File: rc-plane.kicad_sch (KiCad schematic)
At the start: 146 parts, among them IC1 ISLA85005A, IC2 ISLA85005A, J1 POWER, J2 ARMING_PLUG, J3 SMA, J4 E-MATCH_DROGUE, J5 SWD, J6 E-MATCH_RECOVERY, J8 E-MATCH_DROGUE, J9 E-MATCH_RECOVERY, M1 MG90S, M2 MG90S, M3 MG90S, M4 MG90S, M5 MG90S, M6 MG90S, Q1 Q_NMOS_GSD, Q2 Q_NMOS_GSD, Q3 BC547, Q4 Q_NMOS_GSD, Q5 Q_NMOS_GSD, Q6 Q_NMOS_GSD, Q7 Q_NMOS_GSD, Q8 Q_NMOS_GSD, Q9 Q_NMOS_GSD, U1 STM32G474VET6, U5 MP1584EN-LF-Z, U8 MMC5983MA, U9 USBLC6-2SC6, Y1 16MHz

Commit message: Mostly done with schematic, need to do review
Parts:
- removed C2, C3: 100nF, Capacitor_SMD:C_0603_1608Metric, symbol Device:C_Small
- removed C27: 10uF, Capacitor_SMD:C_0603_1608Metric, symbol Device:C
- removed C30, C33: 100nF, Capacitor_SMD:C_0603_1608Metric, symbol Device:C
- removed J9: E-MATCH_RECOVERY, TerminalBlock:TerminalBlock_bornier-2_P5.08mm, symbol Connector:Conn_01x02_Socket
- removed M1, M2, M3, M4, M5, M6: MG90S, Connector_PinHeader_2.54mm:PinHeader_1x03_P2.54mm_Vertical, symbol Motor:Motor_Servo
- removed Q8, Q9: Q_NMOS_GSD, Package_TO_SOT_SMD:TSOT-23, symbol Device:Q_NMOS_GSD
- removed U1: STM32G474VET6, STM32G474VET6:QFP50P1600X1600X160-100N, symbol STM32G474VET6:STM32G474VET6
- removed U8: MMC5983MA, MMC5983MA:PQFN50P300X300X100-16N, symbol MMC5983MA:MMC5983MA
- added C117: 2.2uF, Capacitor_SMD:C_0402_1005Metric, symbol Device:C_Small
- added C27, C30: 100nF, Capacitor_SMD:C_0402_1005Metric, symbol Device:C_Small
- added C33, C42: 100nF, Capacitor_SMD:C_0603_1608Metric, symbol Device:C_Small
- added D10: BLUE, Diode_SMD:D_0603_1608Metric, symbol Device:LED
- added D15, D16: RED_LED, Diode_SMD:D_0603_1608Metric, symbol Device:LED
- added J9: HTSW-109-08-T-T-RA, UCIRP-KiCAD-Lib:SAMTEC_HTSW-109-08-T-T-RA, symbol UCIRP-KiCAD-Lib:HTSW-109-08-T-T-RA
- added U10: RASPBERRY_PI_4B_4GB, UCIRP-KiCAD-Lib:MODULE_RASPBERRY_PI_4B_4GB, symbol UCIRP-KiCAD-Lib:RASPBERRY_PI_4B_4GB
- added U11: ~, Package_QFP:LQFP-64_10x10mm_P0.5mm, symbol UCIRP-KiCAD-Lib:STM32F105RCT6
- added U8: BMM350, 0UCIRP-KiCAD-Lib:BMM350, symbol 0UCIRP-KiCAD-Lib:BMM350
- C34: value 120000uF -> 100nF
- J1: footprint Connector_AMASS:AMASS_XT60-M_1x02_P7.20mm_Vertical -> Connector_AMASS:AMASS_XT60PW-M_1x02_P7.20mm_Horizontal
- R12: value 100k -> 470; Manufacturer (none) -> Generic; Part # (none) -> Generic 0603 470 1% Resistor
- R27, R30: footprint Resistor_SMD:R_0603_1608Metric -> Resistor_SMD:R_0402_1005Metric; Manufacturer (none) -> Generic; Part # (none) -> Generic RES SMD 4.7K OHM 1% 1/4W 0402
- R3: value 3k -> 6k
- R32: value 10k -> 470; footprint (none) -> Resistor_SMD:R_0603_1608Metric; Manufacturer (none) -> Generic; Part # (none) -> Generic 0603 470 1% Resistor
- R40: value 10k -> 100k; Part # Generic 0603 10k 1% Resistor -> Generic 0603 1k 1% Resistor
- R41: value 100 -> 100k; Part # Generic 0603 100 1% Resistor -> Generic 0603 1k 1% Resistor
- R42: value 1 -> 100k; footprint (none) -> Resistor_SMD:R_0603_1608Metric; Manufacturer (none) -> Generic; Part # (none) -> Generic 0603 1k 1% Resistor
- R43: value 10k -> 100k; Manufacturer Generic -> (none); Part # Generic 0603 10k 1% Resistor -> (none)
- R44: value 1k -> 470; Part # Generic 0603 1k 1% Resistor -> Generic 0603 470 1% Resistor
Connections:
- net RADIO_MISO is gone; now on net MEM_MISO: U2.2 (MISO)
- net RADIO_MOSI is gone; now on net MEM_MOSI: U2.3 (MOSI)
- net RADIO_SCK is gone; now on net MEM_SCK: U2.4 (SCK)
- net +3.3V: now also C34.1, R40.2, R41.2, R42.2, R43.2, C27.1, C30.1, C33.1, J9.23, J9.26, U11.1 (VBAT), U11.13 (VDDA), U11.19 (VDD), U11.32 (VDD), U11.48 (VDD), U11.64 (VDD), U8.B3 (VDDIO), U8.C1 (VDD); no longer R12.2, R44.1
- net +5V: now also U10.2 (5V), U10.4 (5V); no longer C10.2, C19.1, C21.1, L1.2, R8.2
- net ALT_CS: now also R40.1, U11.33 (PB12)
- net ALT_MISO: now also U11.35 (PB14)
- net ALT_MOSI: now also U11.36 (PB15)
- net ALT_SCK: now also U11.34 (PB13)
- net ARM_CONT: now also U11.11 (PC3)
- net ARM_POWER: no longer C34.2
- net BATTERY: now also J1.1 (Pin_1)
- net BUZZER: now also U11.37 (PC6)
- net DEBUG_SWCLK: now also U11.49 (PA14)
- net DEBUG_SWDIO: now also U11.46 (PA13)
- net DROGUE: now also U11.8 (PC0); no longer R38.2, R39.1
- net DROGUE_CONT: now also U11.4 (PC15); no longer Q6.3 (D), R35.2
- net GND: now also C34.2, J1.2 (Pin_2), R12.2, C117.2, C27.2, C30.2, C33.2, C42.1, D10.1 (K), J9.03, J9.06, J9.09, J9.12, J9.15, J9.18, J9.21, J9.22, J9.24, J9.25, J9.27, U10.14 (GND), U10.20 (GND), U10.25 (GND), U10.30 (GND), U10.34 (GND), U10.39 (GND), U10.6 (GND), U10.9 (GND), U10.S1 (SHIELD), U10.S2 (SHIELD), U10.S3 (SHIELD), U10.S4 (SHIELD), U11.12 (VSSA), U11.18 (VSS), U11.31 (VSS), U11.47 (VSS), U11.60 (BOOT0), U11.63 (VSS), U8.B1 (GND), U8.B2 (ADSEL), U8.C3 (BYPASS); no longer C34.1, R40.2, R42.2, R43.2
- net GPS_UART_RX: now also U11.59 (PB7)
- net GPS_UART_TX: now also U11.58 (PB6)
- net HSE_IN: now also U11.5 (PD0)
- net IMU_CS1: now also R41.1, U11.24 (PC4)
- net IMU_CS2: now also R42.1, U11.20 (PA4)
- net IMU_MISO: now also U11.23 (PA7)
- net IMU_MOSI: now also U11.22 (PA6)
- net IMU_SCK: now also U11.21 (PA5)
- net LED_ARMED: now also U11.26 (PB0)
- net LED_FLIGHT: now also U11.28 (PB2)
- net LED_STANDBY: now also U11.25 (PC5)
- net LED_STORAGE: now also U11.27 (PB1)
- net MAG_INT: now also U11.40 (PC9), U8.A1 (INT)
- net MAG_SCL: now also U11.61 (PB8), U8.A3 (SCK)
- net MAG_SDA: now also U11.62 (PB9), U8.A2 (SDA)
- net MEM_CS: now also U11.53 (PC12)
- net MEM_HOLD: now also U11.50 (PA15)
- net MEM_MISO: now also U11.56 (PB4)
- net MEM_MOSI: now also U11.57 (PB5)
- net MEM_SCK: now also U11.55 (PB3)
- net MEM_WP: now also U11.43 (PA10)
- net NRST: now also C42.2, U11.7 (~{RST})
- net RECOVERY: now also U11.10 (PC2); no longer R40.1, R41.1
- net RECOVERY_CONT: now also U11.9 (PC1); no longer R44.2
- net USB_D+: now also U11.45 (PA12)
- net USB_D-: now also U11.44 (PA11)
- net VBUS_SENS: now also U11.42 (PA9)
- net at R32.1: now also D15.1 (K)
- net at R43.1: now also IC1. (PHASE_1), D16.2 (A)
- net 5V_EN renamed EN_SERVO
- net 5V_EN_PI renamed EN_PI
- net EN_PI: now also U11.30 (PB11)
- net 5V_PG: no longer names the net of R12.1
- net 5V_PG: now also D16.1 (K); no longer IC1. (PHASE_1)
- net 5V_PG_PI: no longer names the net of IC2. (PHASE_1), R48.1
- net 5V_PG_PI: now also D15.2 (A)
- net RADIO_nCS renamed RADIO_CS
- net RADIO_CS: now also U11.54 (PD2)
- new net: D10.2 (A), R44.2
- new net: R44.1, U10.11 (GPIO17/GPIO_GEN0)
- new net: C117.1, U8.C2 (CRST)
- new net +5V_SERVO: C10.2, C19.1, C21.1, J9.02, J9.05, J9.08, J9.11, J9.14, J9.17, J9.20, L1.2, R8.2
- new net 3V3: U10.1 (3V3), U10.17 (3V3)
- new net AIL_L_PWM3: J9.07, U10.32 (GPIO12), U11.16 (PA2)
- new net AIL_R_PWM4: J9.10, U10.33 (GPIO13), U11.17 (PA3)
- new net BACKUP: R38.2, R39.1, U11.3 (PC14)
- new net BACKUP_CONT: Q6.3 (D), R35.2, U11.2 (PC13)
- new net ELEV_PWM1: J9.01, U10.29 (GPIO5), U11.14 (PA0)
- new net EN_5V: U11.29 (PB10)
- new net ESC_PWM0: J9.19, U10.37 (GPIO26), U11.41 (PA8)
- new net FLAP_L_PWM5: J9.13, U10.38 (GPIO20), U11.38 (PC7)
- new net FLAP_R_PWM6: J9.16, U10.40 (GPIO21), U11.39 (PC8)
- new net PI_UART_RX: U10.8 (GPIO14/TXD0), U11.52 (PC11)
- new net PI_UART_TX: U10.10 (GPIO15/RXD0), U11.51 (PC10)
- new net RUDD_PWM2: J9.04, U10.31 (GPIO6), U11.15 (PA1)
- no-connect marks 48 -> 44
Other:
- note added: "ACD1_IN13"
- note added: "DROGUE, MAIN, AND BACKUP PARACHUTE IGNITION"
- note added: "PLANE INTERCONNECT"
- note added: "RASPBERRY PI 4 INTERCONNECT"
- note added: "SPI1"
- note added: "SPI2"
- note added: "SPI3"
- note added: "USART1"
- note added: "USART3"
- note added: "USB"
- note removed: "DROGUE AND MAIN PARACHUTE IGNITION"
- note removed: "DROGUE AND MAIN PARACHUTE IGNITION BACKUPS"
- note removed: "SERVO CONTROL"
- moved on the sheet: C10, C11, C12, C15, C16, C17, C18, C19, C20, C21, C22, C23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

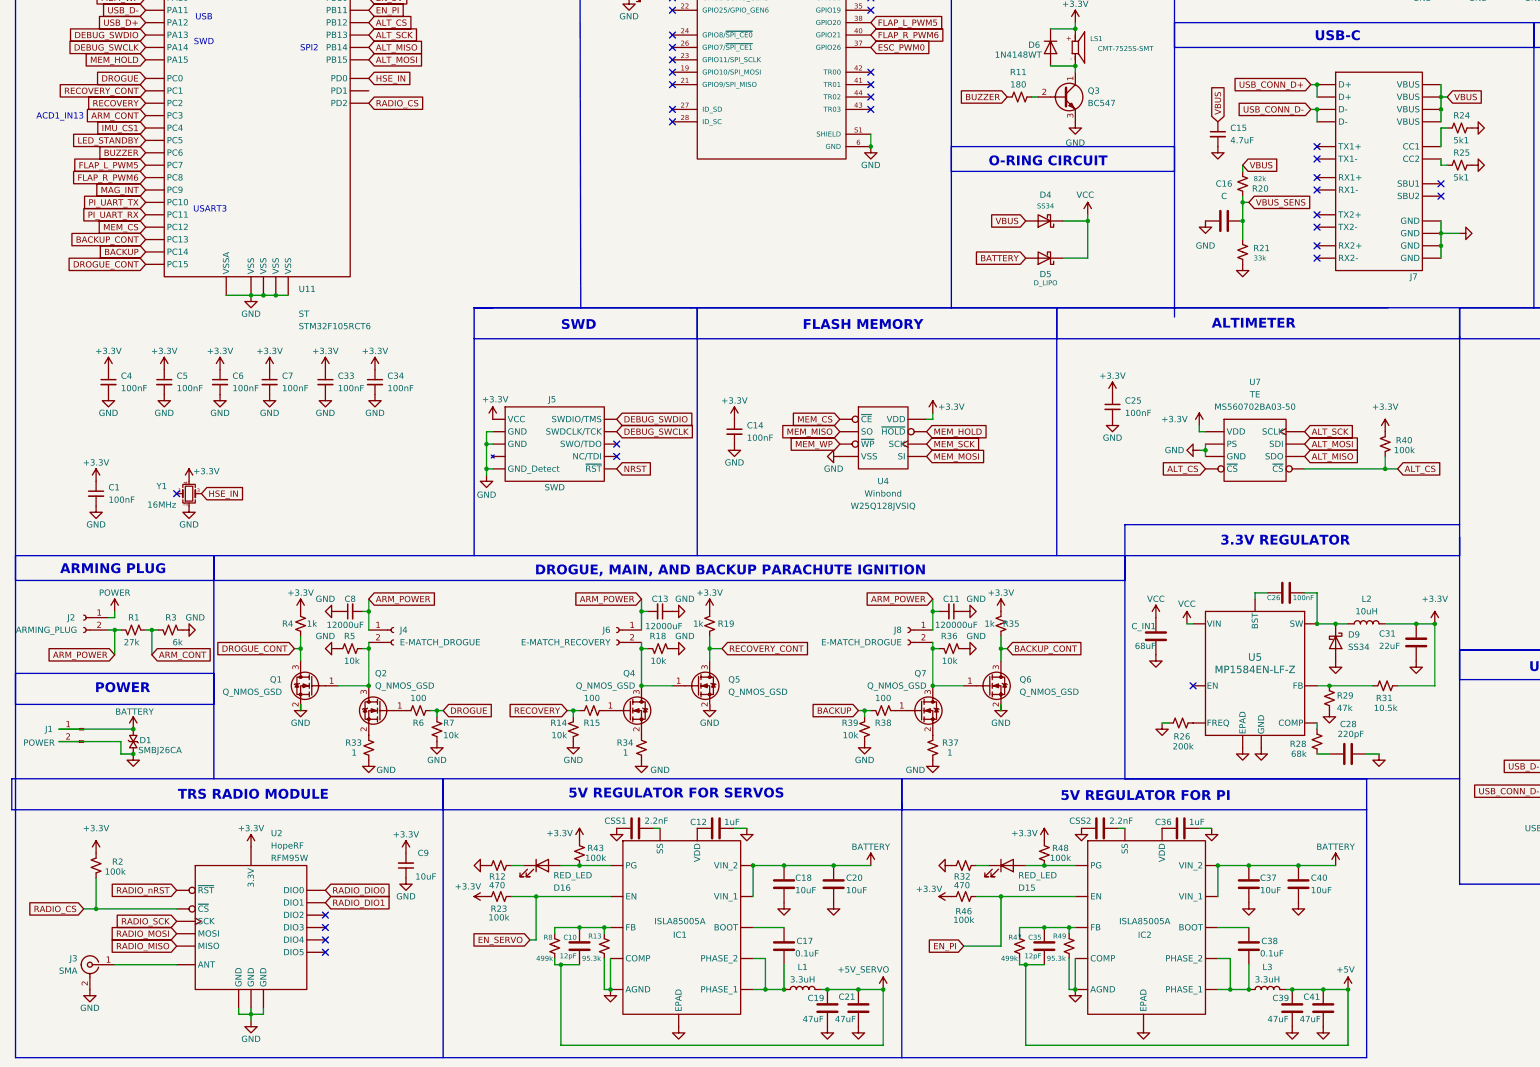
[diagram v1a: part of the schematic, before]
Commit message: made new bucks, only 4 warning/errors when importing from schematic
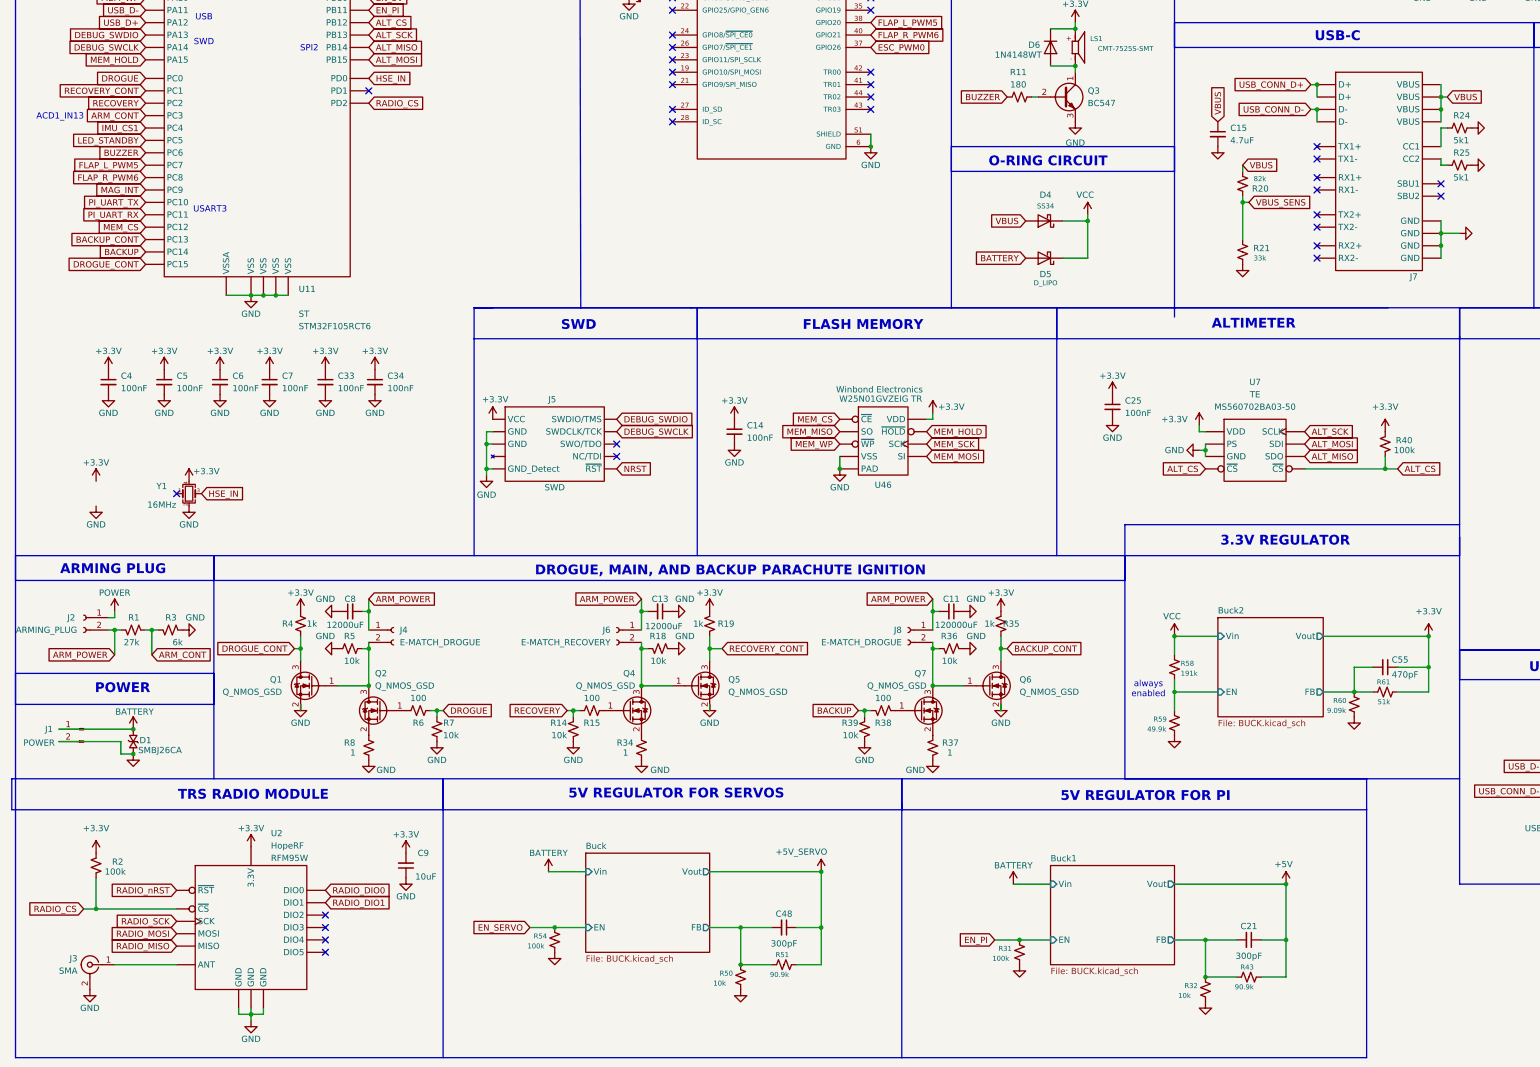
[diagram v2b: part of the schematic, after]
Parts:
- removed C1: 100nF, Capacitor_SMD:C_0603_1608Metric, symbol Device:C_Small
- removed C10, C35: 12pF, Capacitor_SMD:C_0603_1608Metric, symbol Device:C
- removed C12, C36: 1uF, Capacitor_SMD:C_0603_1608Metric, symbol Device:C
- removed C16: C, Capacitor_SMD:C_0603_1608Metric, symbol Device:C
- removed C17, C38: 0.1uF, Capacitor_SMD:C_0603_1608Metric, symbol Device:C
- removed C18, C20, C37, C40: 10uF, Capacitor_SMD:C_0603_1608Metric, symbol Device:C
- removed C19, C21, C39, C41: 47uF, Capacitor_SMD:C_0603_1608Metric, symbol Device:C
- removed C26: 100nF, Capacitor_SMD:C_0603_1608Metric, symbol Device:C
- removed C28: 220pF, Capacitor_SMD:C_0603_1608Metric, symbol Device:C
- removed C31: 22uF, Capacitor_SMD:C_0603_1608Metric, symbol Device:C
- removed CSS1, CSS2: 2.2nF, Capacitor_SMD:C_0603_1608Metric, symbol Device:C
- removed C_IN1: 68uF, Capacitor_SMD:C_0603_1608Metric, symbol Device:C
- removed D15, D16: RED_LED, Diode_SMD:D_0603_1608Metric, symbol Device:LED
- removed D9: SS34, Diode_SMD:D_SMA, symbol Diode:SS34
- removed IC1, IC2: ISLA85005A, KiCad:SON50P300X400X90-13N-D, symbol ISL85005AFRZ-T7A:ISL85005AFRZ-T7A
- removed L1, L3: 3.3uH, Inductor_SMD:L_0603_1608Metric, symbol Device:L
- removed L2: 10uH, Inductor_SMD:L_0603_1608Metric, symbol Device:L
- removed R12: 470, Resistor_SMD:R_0603_1608Metric, symbol Device:R_Small_US
- removed R13, R49: 95.3k, Resistor_SMD:R_0603_1608Metric, symbol Device:R_Small_US
- removed R23, R46, R48: 100k, Resistor_SMD:R_0603_1608Metric, symbol Device:R_Small_US
- removed R26: 200k, Resistor_SMD:R_0603_1608Metric, symbol Device:R_Small_US
- removed R28: 68k, Resistor_SMD:R_0603_1608Metric, symbol Device:R_Small_US
- removed R29: 47k, Resistor_SMD:R_0603_1608Metric, symbol Device:R_Small_US
- removed R33: 1, symbol Device:R_Small_US
- removed R47: 499k, Resistor_SMD:R_0603_1608Metric, symbol Device:R_Small_US
- removed U4: ~, Package_SO:SOIC-8W_5.3x5.3mm_P1.27mm, symbol UCIRP-KiCAD-Lib:SST25VF016B
- removed U5: MP1584EN-LF-Z, MP1584EN:SOIC8E_MPS, symbol 2025-08-17_10-37-18:MP1584EN-LF-Z
- added C21, C48: 300pF, Capacitor_SMD:C_0603_1608Metric, symbol Device:C_Small
- added C55: 470pF, Capacitor_SMD:C_0603_1608Metric, symbol Device:C_Small
- added R50: 10k, Resistor_SMD:R_0603_1608Metric, symbol Device:R_Small_US
- added R51: 90.9k, Resistor_SMD:R_0603_1608Metric, symbol Device:R_Small_US
- added R54: 100k, Resistor_SMD:R_0603_1608Metric, symbol Device:R_Small_US
- added R58: 191k, Resistor_SMD:R_0603_1608Metric, symbol Device:R_Small_US
- added R59: 49.9k, Resistor_SMD:R_0603_1608Metric, symbol Device:R_Small_US
- added R60: 9.09k, Resistor_SMD:R_0603_1608Metric, symbol Device:R_Small_US
- added R61: 51k, Resistor_SMD:R_0603_1608Metric, symbol Device:R_Small_US
- added U46: ~, Package_SON:WSON-8-1EP_8x6mm_P1.27mm_EP3.4x4.3mm, symbol UCIRP-KiCAD-Lib:SST25VF016B
- D1: footprint 1.0SMBJ28CA-Diotec-Semiconductor-Symbol-Kicad-1_3:P26_DO-214AA_SMB -> Diode_SMD:D_SMB
- R31: value 10.5k -> 100k
- R32: value 470 -> 10k; Manufacturer Generic -> (none); Part # Generic 0603 470 1% Resistor -> (none)
- R34, R37, R45: footprint (none) -> Resistor_SMD:R_0603_1608Metric
- R43: value 100k -> 90.9k
- R8: value 499k -> 1
- U2: footprint 0UCIRP-KiCAD-Lib:RFM95W -> UCIRP-KiCAD-Lib:RFM95W
- U8: footprint 0UCIRP-KiCAD-Lib:BMM350 -> UCIRP-KiCAD-Lib:BMM350
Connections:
- net +3.3V: now also C55.1, R61.2, U46.8 (VDD); no longer R31.2, R43.2
- net +5V: now also R43.2, C21.1
- net +5V_SERVO: now also C48.1, R51.2; no longer R8.2
- net BATTERY: now also D1.1; no longer D1.
- net EN_PI: now also R31.1
- net EN_SERVO: now also R54.1
- net GND: now also D1.2, R31.2, R8.2, R50.2, R54.2, R59.2, R60.2, U46.4 (VSS), U46.9 (PAD); no longer D1.
- net MEM_CS: now also U46.1 (~{CE})
- net MEM_HOLD: now also U46.7 (~{HOLD})
- net MEM_MISO: now also U46.2 (SO)
- net MEM_MOSI: now also U46.5 (SI)
- net MEM_SCK: now also U46.6 (SCK)
- net MEM_WP: now also U46.3 (~{WP})
- net VCC: now also R58.1
- net at R8.1: now also Q2.2 (S)
- net Buck1/FB: now reaches R43.1
- net Buck1/FB: now also R32.1, C21.2
- new net Buck/FB: C48.2, R50.1, R51.1
- new net Buck2/EN: R58.2, R59.1
- new net Buck2/FB: C55.2, R60.1, R61.1
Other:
- added sheet Buck (BUCK.kicad_sch)
- added sheet Buck1 (BUCK.kicad_sch)
- added sheet Buck2 (BUCK.kicad_sch)
- note added: "always enabled"
